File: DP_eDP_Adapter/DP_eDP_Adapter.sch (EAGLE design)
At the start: 15 parts, among them IC1 TLC5947XLP, IC2 REG1117M3.3

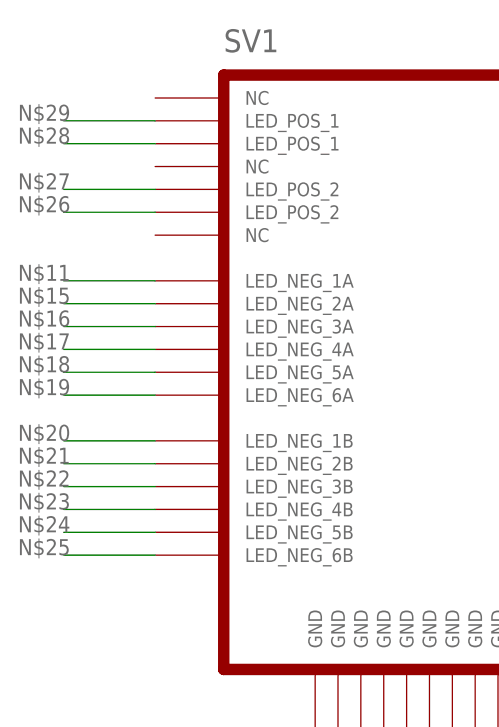
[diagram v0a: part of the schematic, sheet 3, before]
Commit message: 
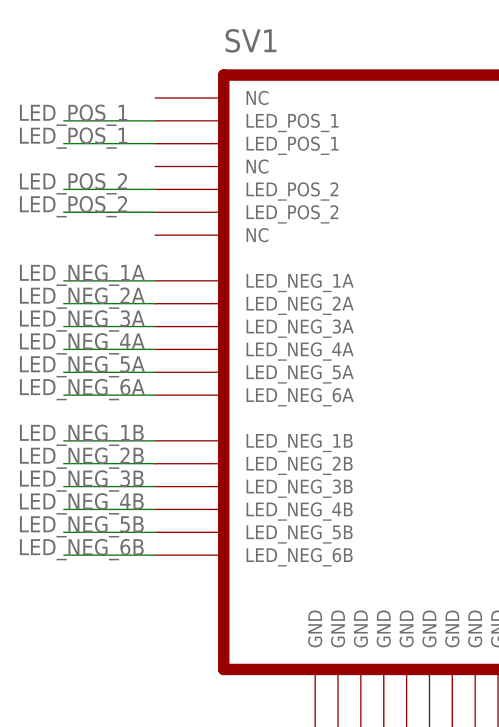
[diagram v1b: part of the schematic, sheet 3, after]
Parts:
- C1, C2: device SparkFun:CAP0603-CAP -> SparkFun:CAP0402-CAP
- R2: device SparkFun-Passives:RESISTOR0603-RES -> SparkFun-Passives:RESISTOR0402-RES
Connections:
- net N$11 renamed LED_NEG_1A
- net N$15 renamed LED_NEG_2A
- net N$16 renamed LED_NEG_3A
- net N$17 renamed LED_NEG_4A
- net N$18 renamed LED_NEG_5A
- net N$19 renamed LED_NEG_6A
- net N$20 renamed LED_NEG_1B
- net N$21 renamed LED_NEG_2B
- net N$22 renamed LED_NEG_3B
- net N$23 renamed LED_NEG_4B
- net N$24 renamed LED_NEG_5B
- net N$25 renamed LED_NEG_6B
- removed net N$26: SV1.LED_POS_2@45
- removed net N$27: SV1.LED_POS_2@46
- removed net N$28: SV1.LED_POS_1@48
- removed net N$29: SV1.LED_POS_1@49
- new net LED_POS_1: SV1.LED_POS_1@48, SV1.LED_POS_1@49
- new net LED_POS_2: SV1.LED_POS_2@45, SV1.LED_POS_2@46

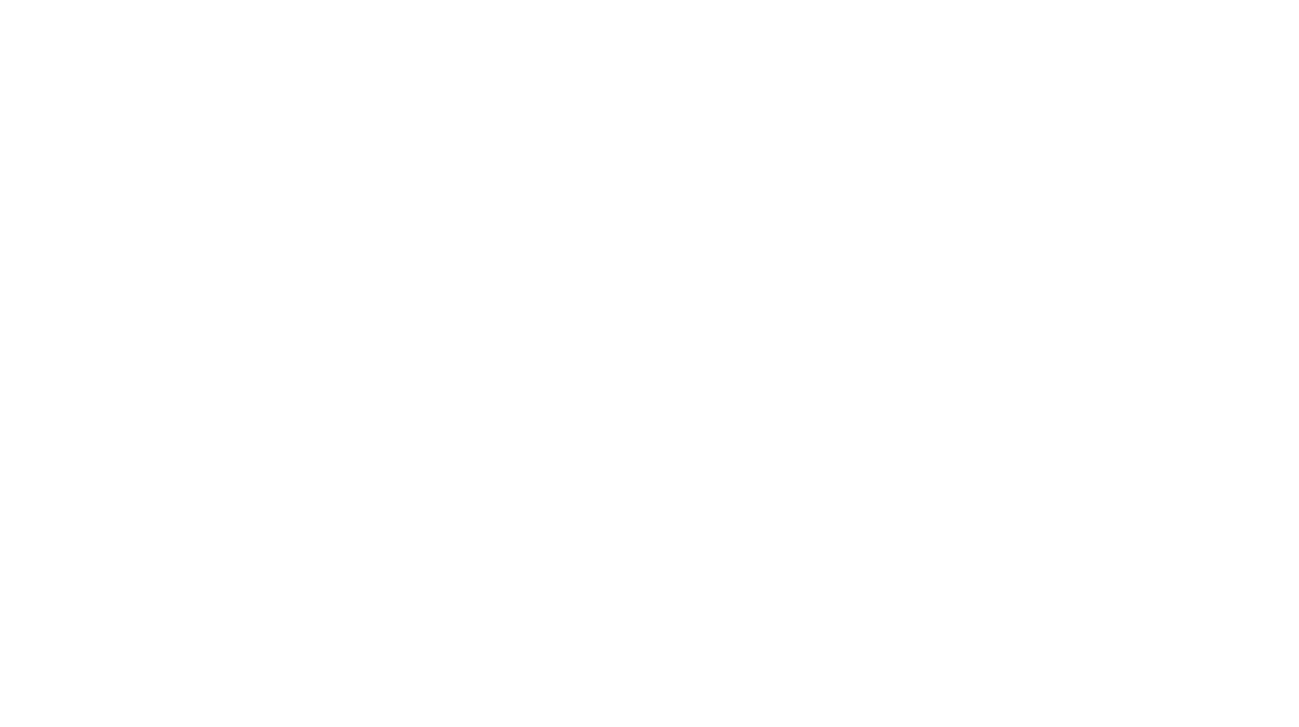
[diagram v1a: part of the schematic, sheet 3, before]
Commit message: 
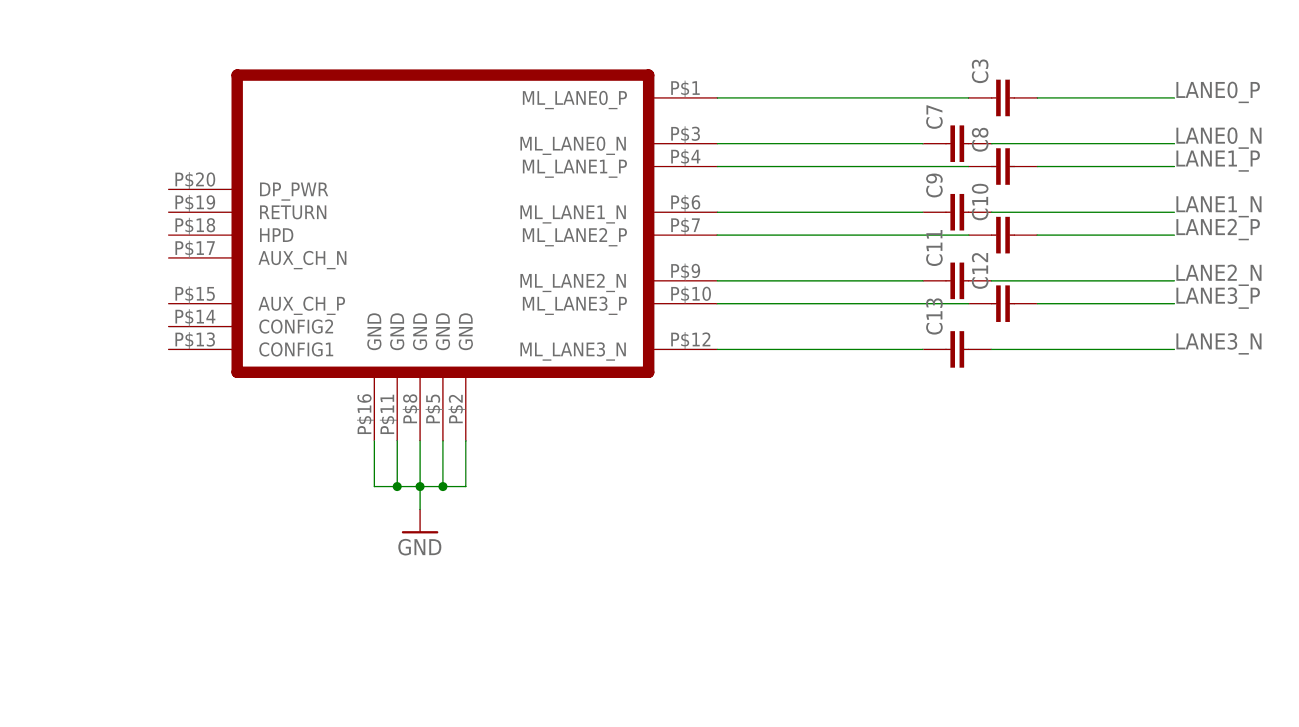
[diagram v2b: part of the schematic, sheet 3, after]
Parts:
- added C10, C11, C12, C13, C3, C7, C8, C9: (no value), DP_eDP_Adapter:SPARKFUN-PASSIVES_CAP0402-CAP
- added JP3: (no value), SparkFun-Connectors:M05PTH
- added U$2: DP1RD20JQ2R400, DP_eDP_Adapter:DP1RD20JQ2R400
- IC2: value REG1117M3.3 -> (none); device burr-brown:REG1117 -> v-reg:78XXS
- JP1: value Power IN -> (none)
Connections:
- new net N$15_N: C9.1, U$2.ML_LANE1_N
- new net N$15_P: C8.1, U$2.ML_LANE1_P
- new net N$17_N: C11.1, U$2.ML_LANE2_N
- new net N$17_P: C10.1, U$2.ML_LANE2_P
- new net N$19_N: C13.1, U$2.ML_LANE3_N
- new net N$19_P: C12.1, U$2.ML_LANE3_P
- new net N$3_N: C7.1, U$2.ML_LANE0_N
- new net N$3_P: C3.1, U$2.ML_LANE0_P
- net +3V3: no longer IC2.VOUT
- net 20V: now also JP3.2, JP3.3; no longer IC2.VIN
- net GND: now also JP3.4, JP3.5, U$2.GND@11, U$2.GND@16, U$2.GND@2, U$2.GND@5, U$2.GND@8; no longer IC2.GND
- net LANE0_N: now also C7.2
- net LANE0_P: now also C3.2
- net LANE1_N: now also C9.2
- net LANE1_P: now also C8.2
- net LANE2_N: now also C11.2
- net LANE2_P: now also C10.2
- net LANE3_N: now also C13.2
- net LANE3_P: now also C12.2

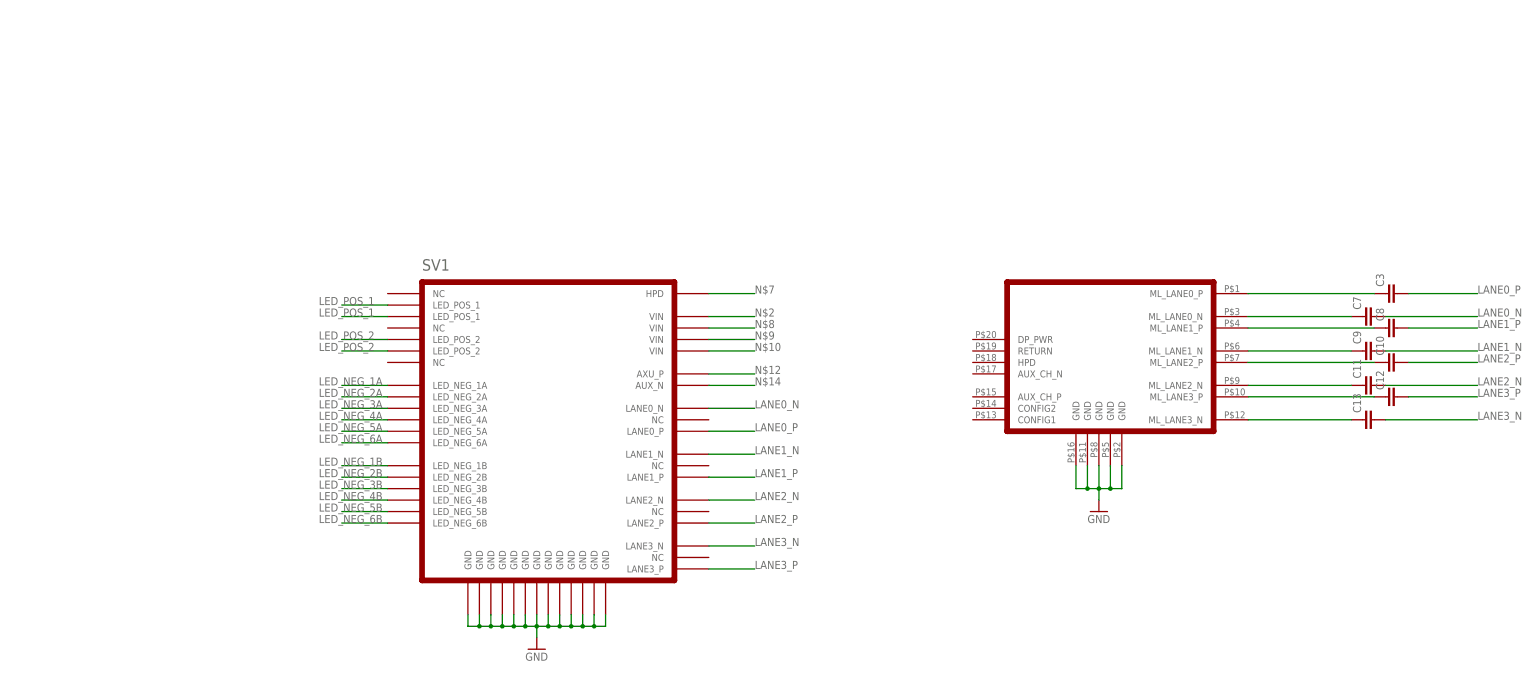
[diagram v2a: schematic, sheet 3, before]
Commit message: 
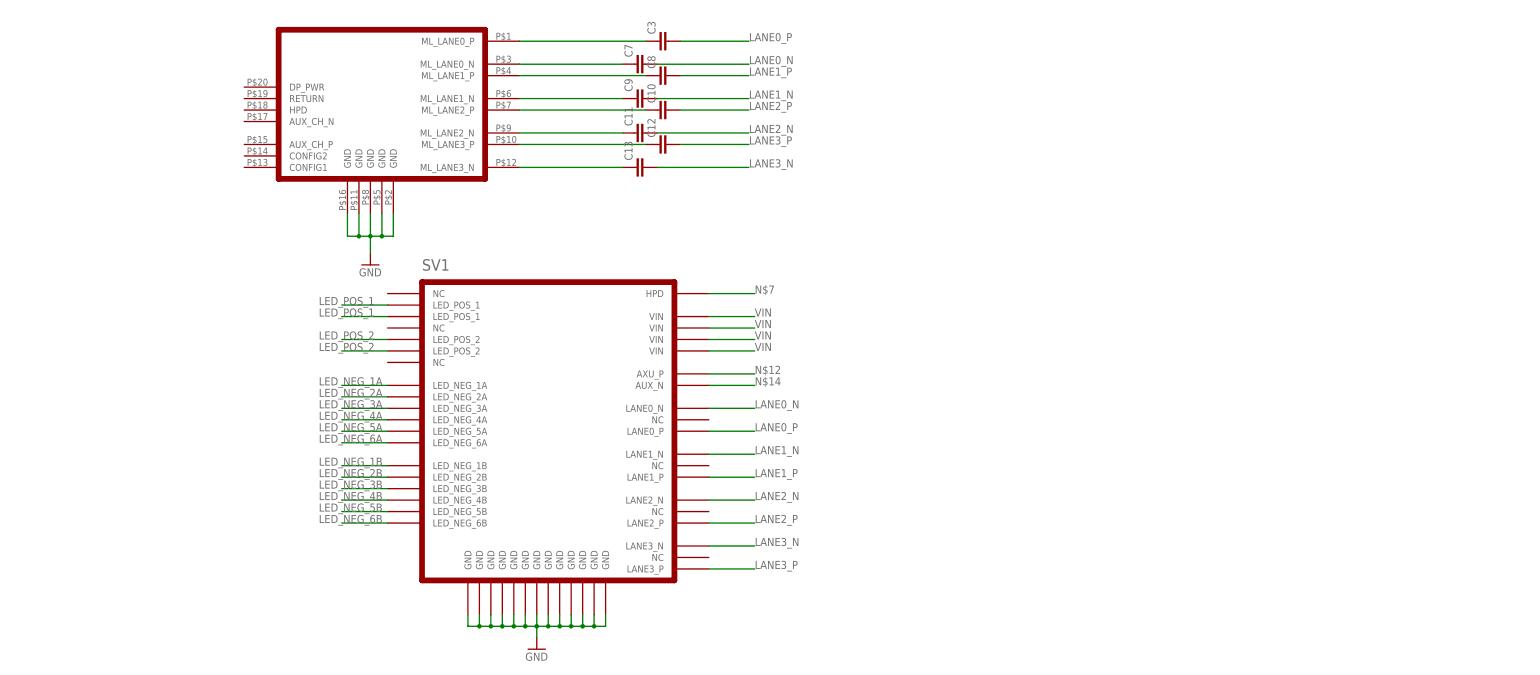
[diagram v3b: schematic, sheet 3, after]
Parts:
- added S1, S2, S3, S4, S5: SWITCH-MOMENTARY-2-SMD-1101NE, SparkFun-Electromechanical:SWITCH-MOMENTARY-2-SMD-1101NE
- C4, C5: device SparkFun-Passives:CAP_POL1206 -> SparkFun-Passives:CAP_POL6032
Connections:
- removed net COL1: IC1.OUT0
- removed net COL10: IC1.OUT9
- removed net COL11: IC1.OUT10
- removed net COL12: IC1.OUT11
- removed net COL13: IC1.OUT12
- removed net COL14: IC1.OUT13
- removed net COL15: IC1.OUT14
- removed net COL16: IC1.OUT15
- removed net COL17: IC1.OUT16
- removed net COL18: IC1.OUT17
- removed net COL19: IC1.OUT18
- removed net COL2: IC1.OUT1
- removed net COL20: IC1.OUT19
- removed net COL21: IC1.OUT20
- removed net COL22: IC1.OUT21
- removed net COL23: IC1.OUT22
- removed net COL24: IC1.OUT23
- removed net COL3: IC1.OUT2
- removed net COL4: IC1.OUT3
- removed net COL5: IC1.OUT4
- removed net COL6: IC1.OUT5
- removed net COL7: IC1.OUT6
- removed net COL8: IC1.OUT7
- removed net COL9: IC1.OUT8
- removed net N$10: SV1.VIN@7
- removed net N$2: SV1.VIN@4
- removed net N$8: SV1.VIN@5
- removed net N$9: SV1.VIN@6
- new net BUTTON_1: S1.1, U$1.(T1)PD5
- new net BUTTON_2: S2.1, U$1.(T0)PD4
- new net BUTTON_3: S3.1, U$1.(INT1)PD3
- new net BUTTON_4: S4.1, U$1.(INT0)PD2
- new net VIN: SV1.VIN@4, SV1.VIN@5, SV1.VIN@6, SV1.VIN@7
- net +3V3: now also IC2.OUT
- net 20V: now also IC2.IN
- net GND: now also IC2.GND, S1.2, S2.2, S3.2, S4.2, S5.1
- net LED_NEG_1A: now also IC1.OUT22, IC1.OUT23
- net LED_NEG_1B: now also IC1.OUT10, IC1.OUT11
- net LED_NEG_2A: now also IC1.OUT20, IC1.OUT21
- net LED_NEG_2B: now also IC1.OUT8, IC1.OUT9
- net LED_NEG_3A: now also IC1.OUT18, IC1.OUT19
- net LED_NEG_3B: now also IC1.OUT6, IC1.OUT7
- net LED_NEG_4A: now also IC1.OUT16, IC1.OUT17
- net LED_NEG_4B: now also IC1.OUT4, IC1.OUT5
- net LED_NEG_5A: now also IC1.OUT14, IC1.OUT15
- net LED_NEG_5B: now also IC1.OUT2, IC1.OUT3
- net LED_NEG_6A: now also IC1.OUT12, IC1.OUT13
- net LED_NEG_6B: now also IC1.OUT0, IC1.OUT1
- net RST: now also S5.2
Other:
- moved on the sheet: C10, C11, C12, C13, C3, C7, C8, C9, SIG_IN, SIG_OUT

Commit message: 
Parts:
- added C14: .1uf, SparkFun-Passives:CAP0402-CAP
- added C15: 0.1uF, SparkFun-Passives:CAP0402-CAP
- added C16, C17: 82pF, SparkFun-Passives:CAP0402-CAP
- added C18: 1000pF, SparkFun-Passives:CAP0402-CAP
- added L1: (no value), rcl:L-US
- added R1: (no value), SparkFun-Passives:RESISTOR0402-RES
- C6: device SparkFun-Passives:CAP0603-CAP -> SparkFun-Passives:CAP0402-CAP
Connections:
- removed net LED_POS_1: SV1.LED_POS_1@48, SV1.LED_POS_1@49
- removed net LED_POS_2: SV1.LED_POS_2@45, SV1.LED_POS_2@46
- new net LED_POS: C17.1, C18.1, L1.2, SV1.LED_POS_1@48, SV1.LED_POS_1@49, SV1.LED_POS_2@45, SV1.LED_POS_2@46
- net 20V: now also C14.1, C15.1, C16.1, L1.1, R1.2
- net GND: now also C14.2, C15.2, C16.2, C17.2, C18.2, R1.1
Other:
- note added: "NEW VALUES"

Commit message: 
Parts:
- added C19, C20, C21, C22, C23, C24, C25, C26, C27: (no value), DP_eDP_Adapter:SPARKFUN-PASSIVES_CAP0402-CAP
- added L2, L3: 240ohm-300ma, rcl:L-US
- added R3, R4, R5: 100K, rcl:R-US_R0402
- C1: value 0.1uF -> .1uf; device SparkFun:CAP0402-CAP -> SparkFun-Passives:CAP0402-CAP
- C10: value (none) -> 82pF; device DP_eDP_Adapter:SPARKFUN-PASSIVES_CAP0402-CAP -> SparkFun-Passives:CAP0402-CAP
- C11, C12: value (none) -> 100pF 50V; device DP_eDP_Adapter:SPARKFUN-PASSIVES_CAP0402-CAP -> SparkFun-Passives:CAP0402-CAP
- C13: value (none) -> 1000pF; device DP_eDP_Adapter:SPARKFUN-PASSIVES_CAP0402-CAP -> SparkFun-Passives:CAP0402-CAP
- C14, C6: value .1uf -> 820pF 50V
- C15: value 0.1uF -> 820pF 50V
- C16, C17: value 82pF -> 0.1uF; device SparkFun-Passives:CAP0402-CAP -> SparkFun:CAP0402-CAP
- C18: value 1000pF -> (none); device SparkFun-Passives:CAP0402-CAP -> DP_eDP_Adapter:SPARKFUN-PASSIVES_CAP0402-CAP
- C2: value 0.1uF -> 10uF 50V; device SparkFun:CAP0402-CAP -> SparkFun-Passives:CAP_POL6032
- C3: value (none) -> 0.1uF; device DP_eDP_Adapter:SPARKFUN-PASSIVES_CAP0402-CAP -> SparkFun-Passives:CAP0402-CAP
- C4: value 10uF -> 100uF 50V
- C5: value 10uF -> 82pF; device SparkFun-Passives:CAP_POL6032 -> SparkFun-Passives:CAP0402-CAP
- C7: value (none) -> 820pF 50V; device DP_eDP_Adapter:SPARKFUN-PASSIVES_CAP0402-CAP -> SparkFun-Passives:CAP0402-CAP
- C8: value (none) -> 10uF; device DP_eDP_Adapter:SPARKFUN-PASSIVES_CAP0402-CAP -> SparkFun-Passives:CAP_POL6032
- C9: value (none) -> .1uf; device DP_eDP_Adapter:SPARKFUN-PASSIVES_CAP0402-CAP -> SparkFun-Passives:CAP0402-CAP
- IC1: value TLC5947XLP -> (none); device slice_noshift:TLC5947XLP -> v-reg:78XXS
- IC2: value (none) -> TLC5947XLP; device v-reg:78XXS -> slice_noshift:TLC5947XLP
- L1: value (none) -> 240ohm-300ma
- SV1: value EDP_CONNECTOR -> (none); device DP_eDP_Adapter:EDP_CONNECTOR -> NSL:MA06-1
- SV2: value (none) -> EDP_CONNECTOR; device NSL:MA06-1 -> DP_eDP_Adapter:EDP_CONNECTOR
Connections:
- removed net LED_POS: C17.1, C18.1, L1.2, SV1.LED_POS_1@48, SV1.LED_POS_1@49, SV1.LED_POS_2@45, SV1.LED_POS_2@46
- removed net N$12: SV1.AXU_P
- removed net N$14: SV1.AUX_N
- removed net N$7: SV1.HPD
- new net AUX_CH_N: C26.1, R3.1, SV2.AUX_N
- new net AUX_CH_P: C27.1, R4.2, SV2.AXU_P
- new net AUX_N: C26.2, U$2.AUX_CH_N
- new net AUX_P: C27.2, U$2.AUX_CH_P
- new net HPD: R5.2, SV2.HPD, U$2.HPD
- new net LED_POS_1: C11.1, C14.1, L2.2, SV2.LED_POS_1@48, SV2.LED_POS_1@49
- new net LED_POS_2: C12.1, C15.1, L3.2, SV2.LED_POS_2@45, SV2.LED_POS_2@46
- net +3V3: now also C16.1, C17.1, C3.1, C5.1, C8.+, C9.1, IC1.OUT, IC2.VCC, L1.1, R1.2, R3.2, SV1.4; no longer C2.1, C5.+, C6.1, IC1.VCC, IC2.OUT, SV2.4
- net 20V: now also C2.+, C6.1, C7.1, IC1.IN, L2.1, L3.1; no longer C14.1, C15.1, C16.1, IC2.IN, L1.1, R1.2
- net BLANK: now also IC2.BLANK; no longer IC1.BLANK
- net BUTTON_1: now also S2.1; no longer S1.1
- net BUTTON_2: now also S3.1; no longer S2.1
- net BUTTON_3: now also S4.1; no longer S3.1
- net BUTTON_4: now also S5.1; no longer S4.1
- net GND: now also C10.2, C11.2, C12.2, C13.2, C2.-, C3.2, C5.2, C7.2, C8.-, C9.2, R4.1, R5.1, S1.1, S5.2, SV1.6, SV2.GND@1, SV2.GND@11, SV2.GND@15, SV2.GND@19, SV2.GND@23, SV2.GND@27, SV2.GND@28, SV2.GND@29, SV2.GND@3, SV2.GND@36, SV2.GND@43, SV2.GND@51, SV2.GND@8; no longer C18.2, C2.2, C5.-, S1.2, S5.1, SV1.GND@1, SV1.GND@11, SV1.GND@15, SV1.GND@19, SV1.GND@23, SV1.GND@27, SV1.GND@28, SV1.GND@29, SV1.GND@3, SV1.GND@36, SV1.GND@43, SV1.GND@51, SV1.GND@8, SV2.6
- net LANE0_N: now also C18.2, SV2.LANE0_N; no longer C7.2, SV1.LANE0_N
- net LANE0_P: now also C22.2, SV2.LANE0_P; no longer C3.2, SV1.LANE0_P
- net LANE1_N: now also C19.2, SV2.LANE1_N; no longer C9.2, SV1.LANE1_N
- net LANE1_P: now also C23.2, SV2.LANE1_P; no longer C8.2, SV1.LANE1_P
- net LANE2_N: now also C20.2, SV2.LANE2_N; no longer C11.2, SV1.LANE2_N
- net LANE2_P: now also C24.2, SV2.LANE2_P; no longer C10.2, SV1.LANE2_P
- net LANE3_N: now also C21.2, SV2.LANE3_N; no longer C13.2, SV1.LANE3_N
- net LANE3_P: now also C25.2, SV2.LANE3_P; no longer C12.2, SV1.LANE3_P
- net LED_NEG_1A: now also IC2.OUT22, IC2.OUT23, SV2.LED_NEG_1A; no longer IC1.OUT22, IC1.OUT23, SV1.LED_NEG_1A
- net LED_NEG_1B: now also IC2.OUT10, IC2.OUT11, SV2.LED_NEG_1B; no longer IC1.OUT10, IC1.OUT11, SV1.LED_NEG_1B
- net LED_NEG_2A: now also IC2.OUT20, IC2.OUT21, SV2.LED_NEG_2A; no longer IC1.OUT20, IC1.OUT21, SV1.LED_NEG_2A
- net LED_NEG_2B: now also IC2.OUT8, IC2.OUT9, SV2.LED_NEG_2B; no longer IC1.OUT8, IC1.OUT9, SV1.LED_NEG_2B
- net LED_NEG_3A: now also IC2.OUT18, IC2.OUT19, SV2.LED_NEG_3A; no longer IC1.OUT18, IC1.OUT19, SV1.LED_NEG_3A
- net LED_NEG_3B: now also IC2.OUT6, IC2.OUT7, SV2.LED_NEG_3B; no longer IC1.OUT6, IC1.OUT7, SV1.LED_NEG_3B
- net LED_NEG_4A: now also IC2.OUT16, IC2.OUT17, SV2.LED_NEG_4A; no longer IC1.OUT16, IC1.OUT17, SV1.LED_NEG_4A
- net LED_NEG_4B: now also IC2.OUT4, IC2.OUT5, SV2.LED_NEG_4B; no longer IC1.OUT4, IC1.OUT5, SV1.LED_NEG_4B
- net LED_NEG_5A: now also IC2.OUT14, IC2.OUT15, SV2.LED_NEG_5A; no longer IC1.OUT14, IC1.OUT15, SV1.LED_NEG_5A
- net LED_NEG_5B: now also IC2.OUT2, IC2.OUT3, SV2.LED_NEG_5B; no longer IC1.OUT2, IC1.OUT3, SV1.LED_NEG_5B
- net LED_NEG_6A: now also IC2.OUT12, IC2.OUT13, SV2.LED_NEG_6A; no longer IC1.OUT12, IC1.OUT13, SV1.LED_NEG_6A
- net LED_NEG_6B: now also IC2.OUT0, IC2.OUT1, SV2.LED_NEG_6B; no longer IC1.OUT0, IC1.OUT1, SV1.LED_NEG_6B
- net MISO: now also SV1.2; no longer SV2.2
- net MOSI: now also SV1.1; no longer SV2.1
- net N$13: now also IC2.IREF; no longer IC1.IREF
- net N$15_N: now also C19.1; no longer C9.1
- net N$15_P: now also C23.1; no longer C8.1
- net N$17_N: now also C20.1; no longer C11.1
- net N$17_P: now also C24.1; no longer C10.1
- net N$19_N: now also C21.1; no longer C13.1
- net N$19_P: now also C25.1; no longer C12.1
- net N$3_N: now also C18.1; no longer C7.1
- net N$3_P: now also C22.1; no longer C3.1
- net RST: now also S1.2, SV1.5; no longer S5.2, SV2.5
- net SCK: now also SV1.3; no longer SV2.3
- net SCLK: now also IC2.SCLK; no longer IC1.SCLK
- net SIN: now also IC2.SIN; no longer IC1.SIN
- net SOUT: now also IC2.SOUT; no longer IC1.SOUT
- net VIN: now also C10.1, C13.1, L1.2, SV2.VIN@4, SV2.VIN@5, SV2.VIN@6, SV2.VIN@7; no longer SV1.VIN@4, SV1.VIN@5, SV1.VIN@6, SV1.VIN@7
- net XLAT: now also IC2.XLAT; no longer IC1.XLAT
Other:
- note removed: "NEW VALUES"
